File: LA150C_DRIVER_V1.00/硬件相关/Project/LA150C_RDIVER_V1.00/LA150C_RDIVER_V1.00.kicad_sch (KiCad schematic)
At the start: 9 parts, among them J1 DF52-4P-0.8C, J2 SWD-1X5-1.27

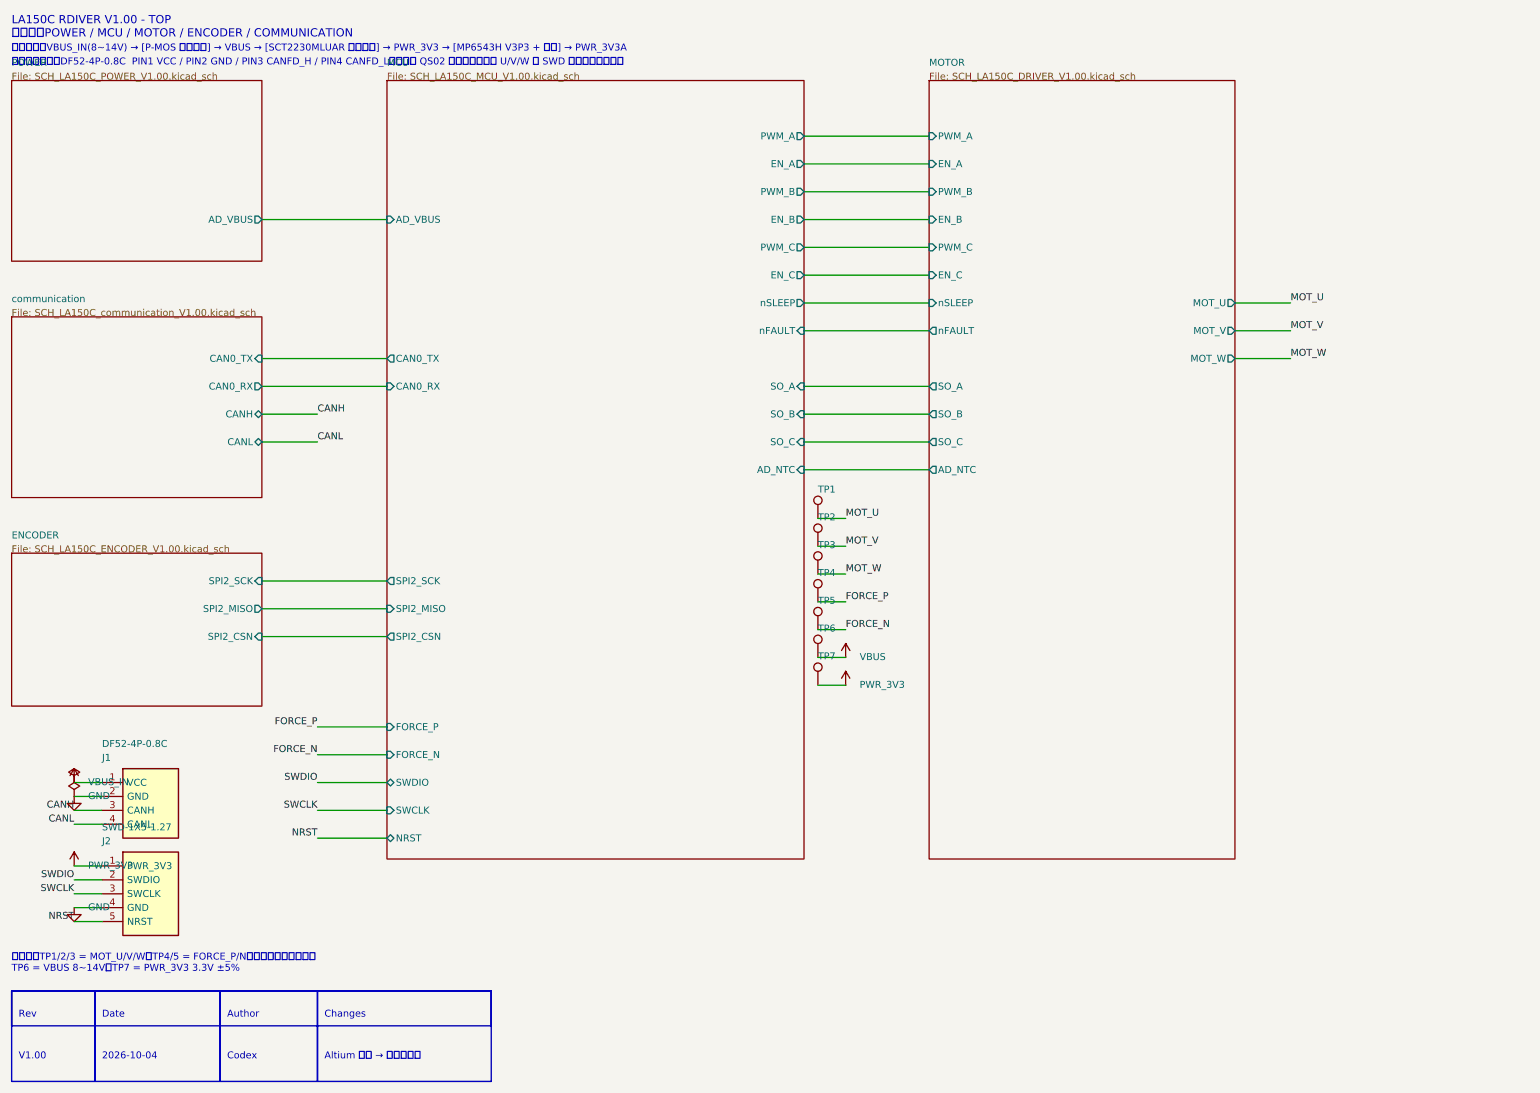
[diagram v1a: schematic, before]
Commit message: feat: finalize LA150C driver schematic
Align the GD32F503 BGA64 pin resources with QS01 V1.12, retain the SCT2230, MT6701 and CAN FD circuits, replace the motor test points with 1.0 x 2.0 mm solder pads, and update the symbols, footprints, ERC report, netlist, BOM and PDF.
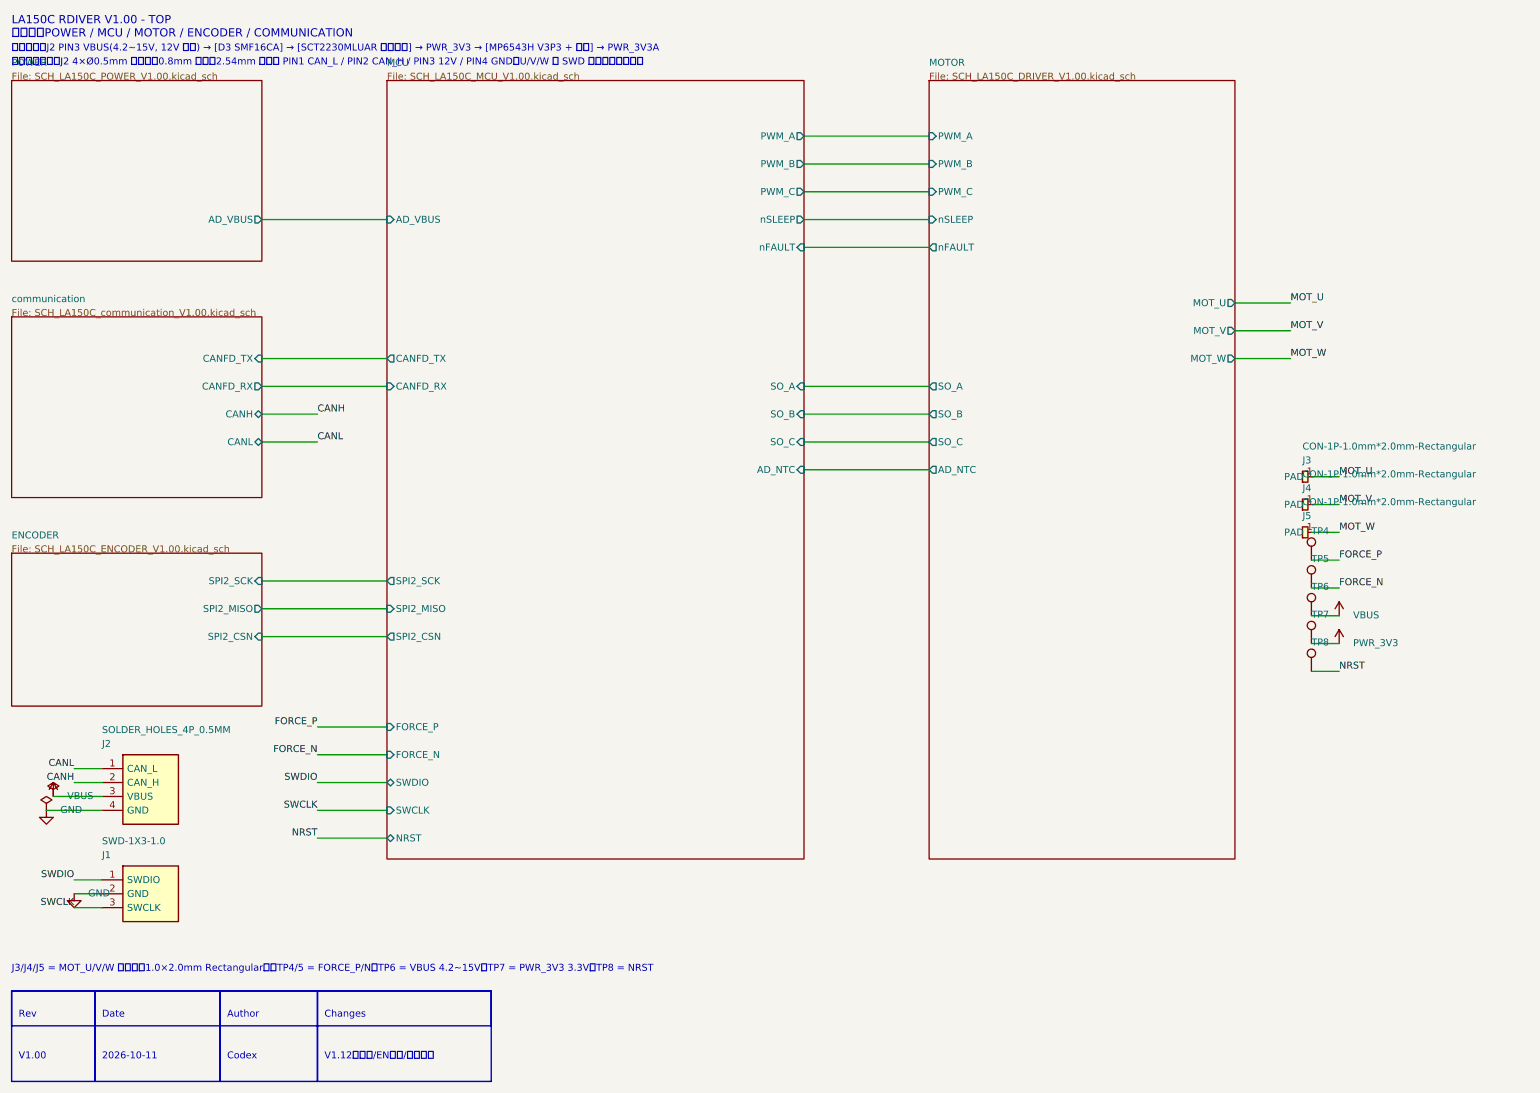
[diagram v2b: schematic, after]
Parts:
- removed TP1, TP2, TP3: TP0.8, TestPoint:TestPoint_Pad_D1.0mm, symbol Connector:TestPoint
- added J3, J4, J5: CON-1P-1.0mm*2.0mm-Rectangular, LA150C_RDIVER_V1.00:CON-1P-1.0mmx2.0mm-Rectangular, symbol LA150C_RDIVER_V1.00:CON-1P-1.0mmx2.0mm-Rectangular
- added TP8: TP0.8, TestPoint:TestPoint_Pad_D1.0mm, symbol Connector:TestPoint
- J1: value DF52-4P-0.8C -> SWD-1X3-1.0; footprint (none) -> Connector_PinHeader_1.00mm:PinHeader_1x03_P1.00mm_Vertical; symbol LA150C_RDIVER_V1.00:DF52-4P-0.8C -> LA150C_RDIVER_V1.00:SWD-1X3-1.0; MPN DF52-4P-0.8C -> SWD-1X3-1.0; Manufacturer Hirose -> (none)
- J2: value SWD-1X5-1.27 -> SOLDER_HOLES_4P_0.5MM; footprint (none) -> LA150C_RDIVER_V1.00:Solder_Holes_4P_0.5mm; symbol LA150C_RDIVER_V1.00:SWD-1X5-1.27 -> LA150C_RDIVER_V1.00:SOLDER_HOLES_4P_0.5MM; MPN SWD-1X5-1.27 -> SOLDER_HOLES_4P_0.5MM
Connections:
- net VBUS_IN is gone; now on net SWDIO: J1.1 (SWDIO)
- net CANH: now also J2.2 (CAN_H); no longer J1.3 (CANH)
- net CANL: now also J2.1 (CAN_L); no longer J1.4 (CANL)
- net MOT_U: now also J3.1 (PAD)
- net MOT_V: now also J4.1 (PAD)
- net MOT_W: now also J5.1 (PAD)
- net NRST: now also TP8.1; no longer J2.5 (NRST)
- net PWR_3V3: no longer J2.1 (PWR_3V3)
- net SWCLK: now also J1.3 (SWCLK); no longer J2.3 (SWCLK)
- net SWDIO: no longer J2.2 (SWDIO)
- net VBUS: now also J2.3 (VBUS)
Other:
- sheet MCU ports: added CANFD_RX, CANFD_TX; removed CAN0_RX, CAN0_TX, EN_A, EN_B, EN_C
- sheet MOTOR ports: added none; removed EN_A, EN_B, EN_C
- sheet communication ports: added CANFD_RX, CANFD_TX; removed CAN0_RX, CAN0_TX
- note added: "2026-10-11"
- note added: "J3/J4/J5 = MOT_U/V/W 焊接盘（1.0×2.0mm Rectangular）；TP4/5 = FORCE_P/N；TP6 = VBUS 4.2~15V；TP7 = PWR_3V3 3.3V；TP8 = NRST"
- note added: "V1.12资源表/EN上拉/外置晶振"
- note added: "整机对外接口：J2 4×Ø0.5mm 焊接孔（0.8mm 外径，2.54mm 间距） PIN1 CAN_L / PIN2 CAN_H / PIN3 12V / PIN4 GND；U/V/W 与 SWD 不引出到该连接器"
- note added: "电源流向：J2 PIN3 VBUS(4.2~15V, 12V 额定) → [D3 SMF16CA] → [SCT2230MLUAR 同步降压] → PWR_3V3 → [MP6543H V3P3 + 磁珠] → PWR_3V3A"
- note removed: "2026-10-04"
- note removed: "Altium 导入 → 脚本化重绘"
- note removed: "整机对外接口：DF52-4P-0.8C PIN1 VCC / PIN2 GND / PIN3 CANFD_H / PIN4 CANFD_L（线序与 QS02 规格书一致）； U/V/W 与 SWD 不引出到该连接器"
- note removed: "测试点：TP1/2/3 = MOT_U/V/W；TP4/5 = FORCE_P/N（一维力传感器预留） TP6 = VBUS 8~14V；TP7 = PWR_3V3 3.3V ±5%"
- note removed: "电源流向：VBUS_IN(8~14V) → [P-MOS 反接保护] → VBUS → [SCT2230MLUAR 同步降压] → PWR_3V3 → [MP6543H V3P3 + 磁珠] → PWR_3V3A"
- moved on the sheet: TP4, TP5, TP6, TP7
